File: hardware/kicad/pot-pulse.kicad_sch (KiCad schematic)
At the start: 57 parts, among them J1 USB-C POWER + NATIVE USB, J2 ZONE 1 SEN0193, J3 ZONE 2 SEN0193, J4 ZONE 3 SEN0193, J5 ZONE 4 SEN0193, J6 DEBUG / PROGRAM PADS, U1 TPS62162DSGR 3.3V, U2 ESP32-C3-MINI-1-H4X, U3 TPD4E05U06DQAR, U4 ADS1115IDGSR, U5 SHT40-AD1B-R2, U6 VEML7700-TR, U7 USBLC6-2SC6

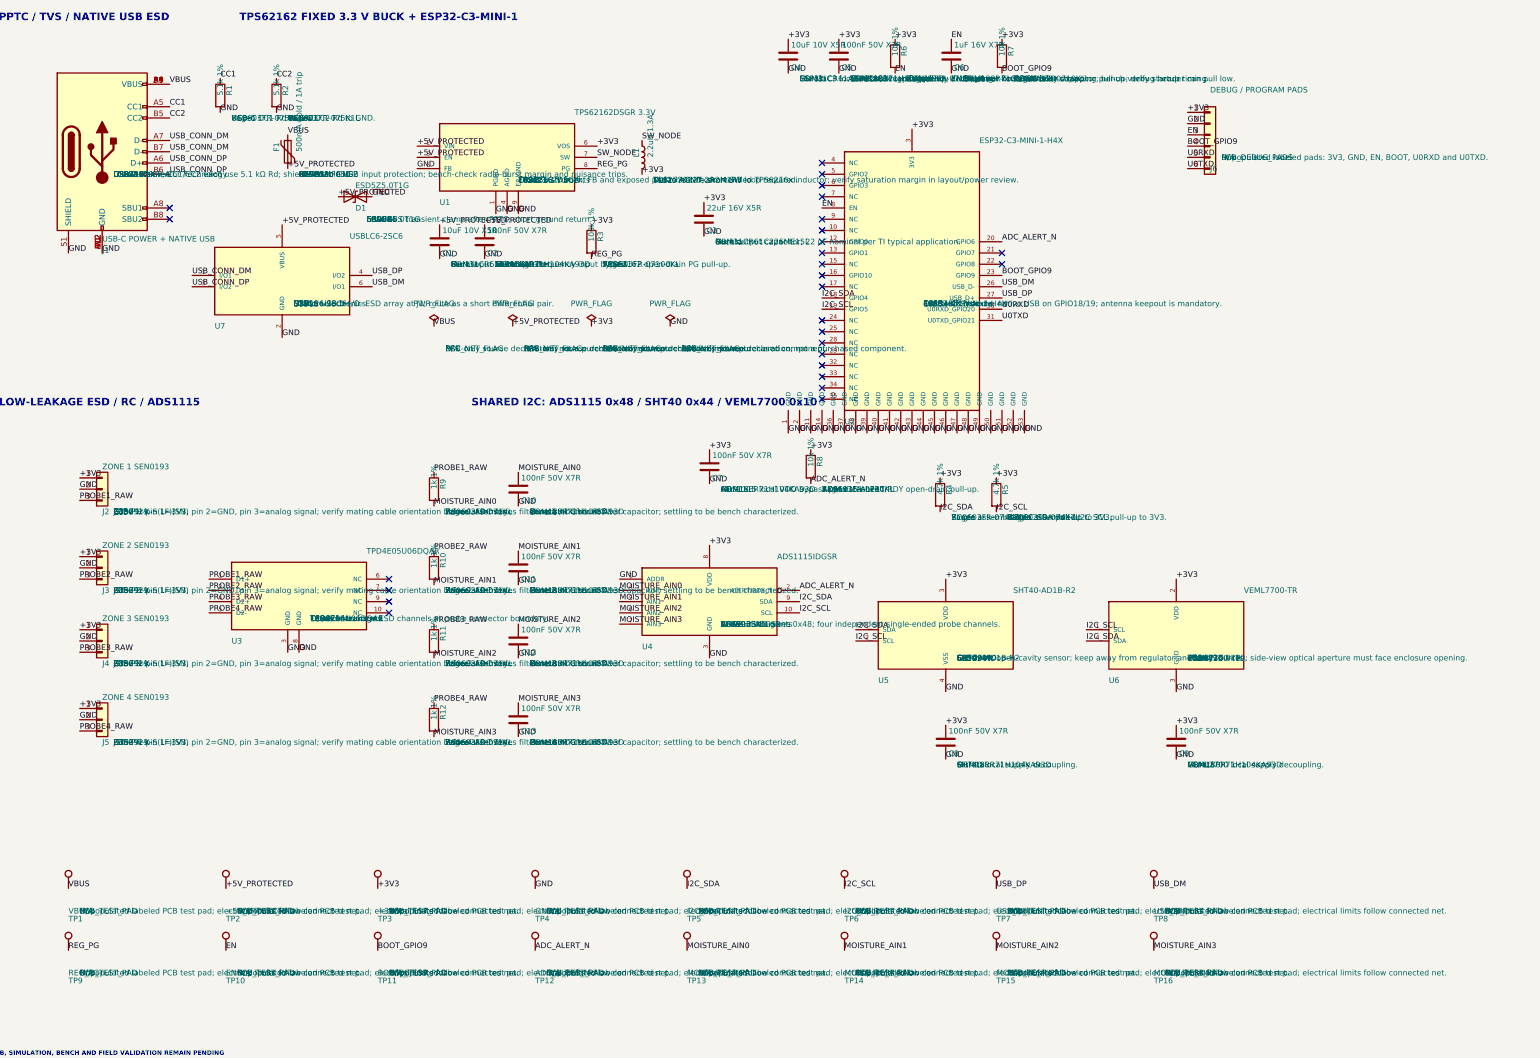
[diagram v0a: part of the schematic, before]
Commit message: feat(bom): add schematic-owned BOM pipeline (#12)
Export grouped board parts from KiCad symbol properties, track
non-schematic procurement items, and validate reproducibility and
field completeness with explicit dated-price evidence.

Co-authored-by: rwrife <rwrife@users.noreply.github.com>
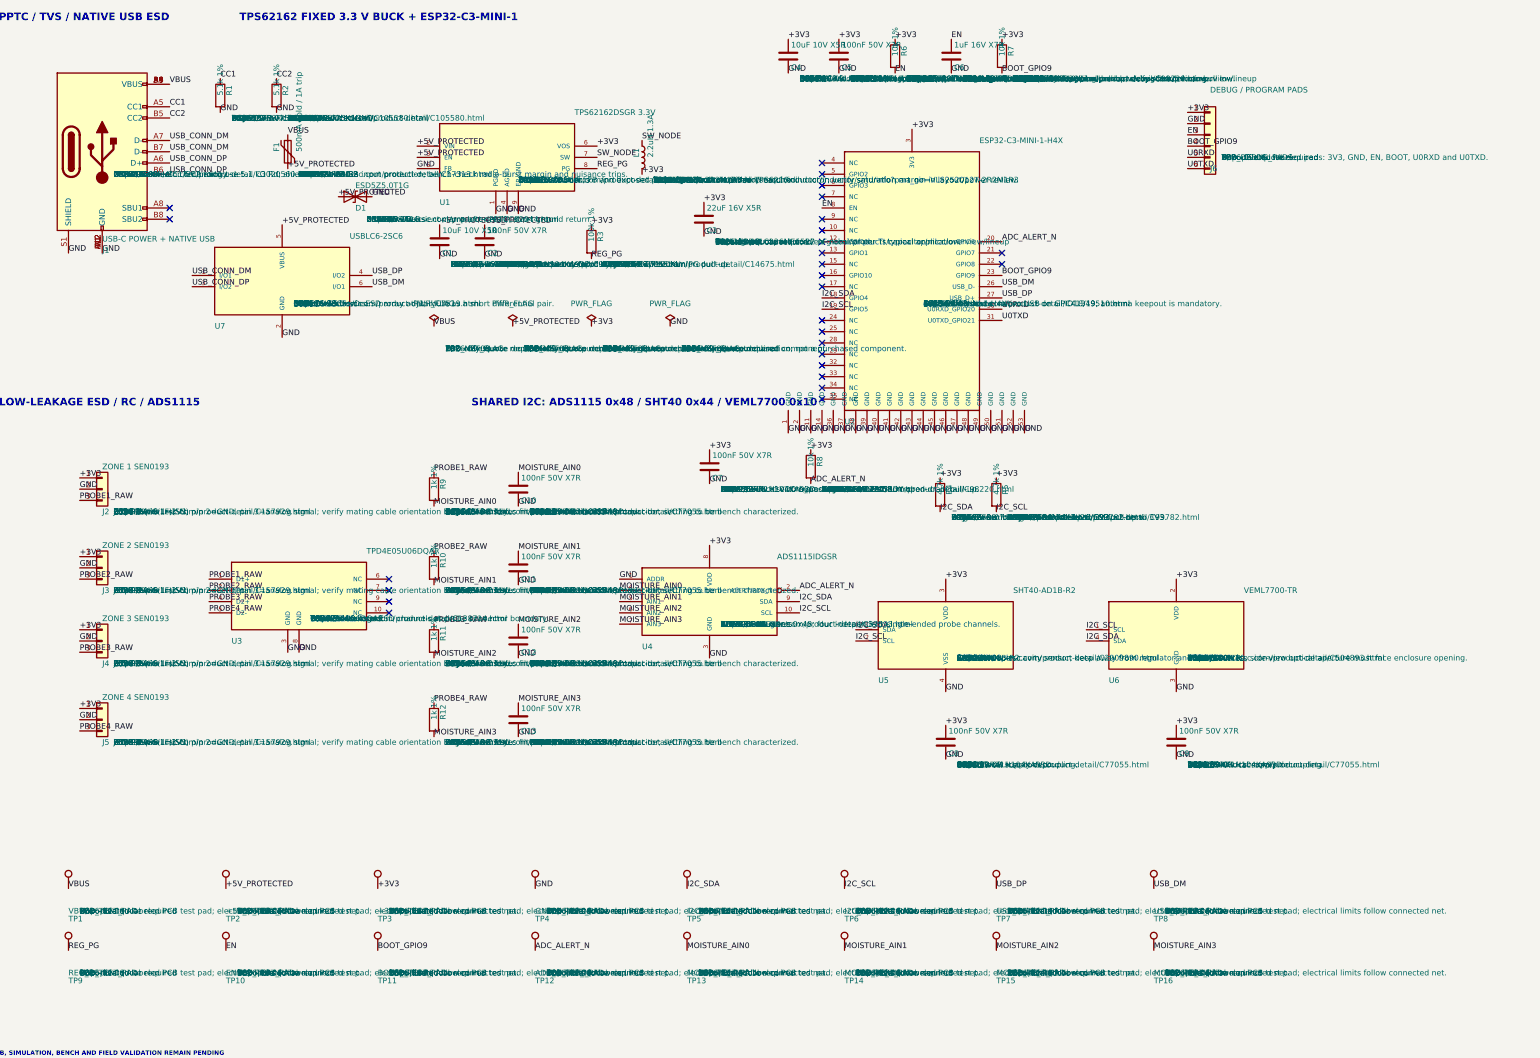
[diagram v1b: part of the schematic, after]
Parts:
- C1, C4: Estimated Unit Cost USD (none) -> 0.3352; Price Snapshot Date (none) -> 2026-09-08; Source URL (none) -> https://www.lcsc.com/product-detail/C97949.html; Supplier (none) -> LCSC; Supplier PN (none) -> C97949
- C10, C11, C12, C13, C2, C5, C7, C8, C9: Estimated Unit Cost USD (none) -> 0.0199; Price Snapshot Date (none) -> 2026-09-08; Source URL (none) -> https://www.lcsc.com/product-detail/C77055.html; Supplier (none) -> LCSC; Supplier PN (none) -> C77055
- C3, C6: Estimated Unit Cost USD (none) -> TBD - live quote required; Price Snapshot Date (none) -> 2026-09-08; Source URL (none) -> https://www.murata.com/en-global/products/capacitor/mlcc/ov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; Supplier (none) -> Unassigned
- D1: Estimated Unit Cost USD (none) -> 0.0365; Price Snapshot Date (none) -> 2026-09-08; Source URL (none) -> https://www.lcsc.com/product-detail/C82044.html
- F1: Estimated Unit Cost USD (none) -> 0.0690; Price Snapshot Date (none) -> 2026-09-08; Source URL (none) -> https://www.lcsc.com/product-detail/C17313.html
- J1: Estimated Unit Cost USD (none) -> 1.0319; Price Snapshot Date (none) -> 2026-09-08; Source URL (none) -> https://www.lcsc.com/product-detail/C3020560.html
- J2, J3, J4, J5: Estimated Unit Cost USD (none) -> 0.0497; Price Snapshot Date (none) -> 2026-09-08; Source URL (none) -> https://www.lcsc.com/product-detail/C157929.html
- J6, TP1, TP10, TP11, TP12, TP13, TP14, TP15, TP16, TP2, TP3, TP4, TP5, TP6, TP7, TP8, TP9: Estimated Unit Cost USD (none) -> TBD - live quote required; Price Snapshot Date (none) -> 2026-09-08
- L1: Estimated Unit Cost USD (none) -> TBD - live quote required; Price Snapshot Date (none) -> 2026-09-08; Source URL (none) -> https://product.tdk.com/en/search/inductor/inductor/smd/inf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; Supplier (none) -> Unassigned
- R1, R2: Estimated Unit Cost USD (none) -> 0.0020; Price Snapshot Date (none) -> 2026-09-08; Source URL (none) -> https://www.lcsc.com/product-detail/C105580.html; Supplier (none) -> LCSC; Supplier PN (none) -> C105580
- R10, R11, R12, R9: Estimated Unit Cost USD (none) -> 0.0021; Price Snapshot Date (none) -> 2026-09-08; Source URL (none) -> https://www.lcsc.com/product-detail/C22548.html; Supplier (none) -> LCSC; Supplier PN (none) -> C22548
- R3: Estimated Unit Cost USD (none) -> 0.0022; Price Snapshot Date (none) -> 2026-09-08; Source URL (none) -> https://www.lcsc.com/product-detail/C14675.html; Supplier (none) -> LCSC; Supplier PN (none) -> C14675
- R4, R5: Estimated Unit Cost USD (none) -> 0.0023; Price Snapshot Date (none) -> 2026-09-08; Source URL (none) -> https://www.lcsc.com/product-detail/C99782.html; Supplier (none) -> LCSC; Supplier PN (none) -> C99782
- R6, R7, R8: Estimated Unit Cost USD (none) -> 0.0023; Price Snapshot Date (none) -> 2026-09-08; Source URL (none) -> https://www.lcsc.com/product-detail/C98220.html; Supplier (none) -> LCSC; Supplier PN (none) -> C98220
- U1: Estimated Unit Cost USD (none) -> 0.9697; Price Snapshot Date (none) -> 2026-09-08; Source URL (none) -> https://www.lcsc.com/product-detail/C40256.html
- U2: Estimated Unit Cost USD (none) -> 3.0795; Price Snapshot Date (none) -> 2026-09-08; Source URL (none) -> https://www.lcsc.com/product-detail/C41349510.html
- U3: Estimated Unit Cost USD (none) -> 0.0819; Price Snapshot Date (none) -> 2026-09-05; Source URL (none) -> https://www.lcsc.com/product-detail/C138714.html
- U4: Estimated Unit Cost USD (none) -> 1.5342; Price Snapshot Date (none) -> 2026-09-08; Source URL (none) -> https://www.lcsc.com/product-detail/C37593.html
- U5: Estimated Unit Cost USD (none) -> 2.0288; Price Snapshot Date (none) -> 2026-09-08; Source URL (none) -> https://www.lcsc.com/product-detail/C2909890.html
- U6: Estimated Unit Cost USD (none) -> 0.7256; Price Snapshot Date (none) -> 2026-09-08; Source URL (none) -> https://www.lcsc.com/product-detail/C504893.html
- U7: Estimated Unit Cost USD (none) -> 0.1639; Price Snapshot Date (none) -> 2026-09-05; Source URL (none) -> https://www.lcsc.com/product-detail/C7519.html
